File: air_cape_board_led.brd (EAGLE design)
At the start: 100 x 80 mm, 10 parts

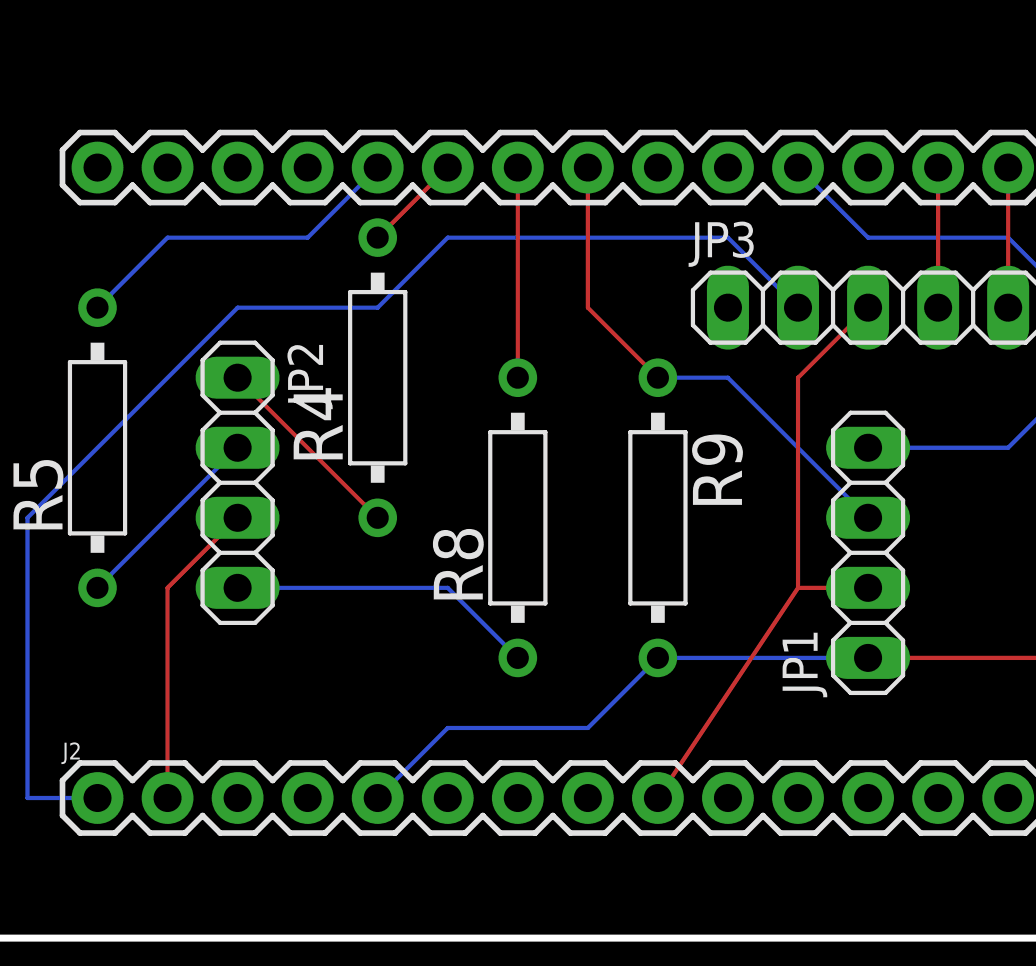
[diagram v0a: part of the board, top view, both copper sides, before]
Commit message: Fix issue with led power supply
- Should be VDD instead of GND
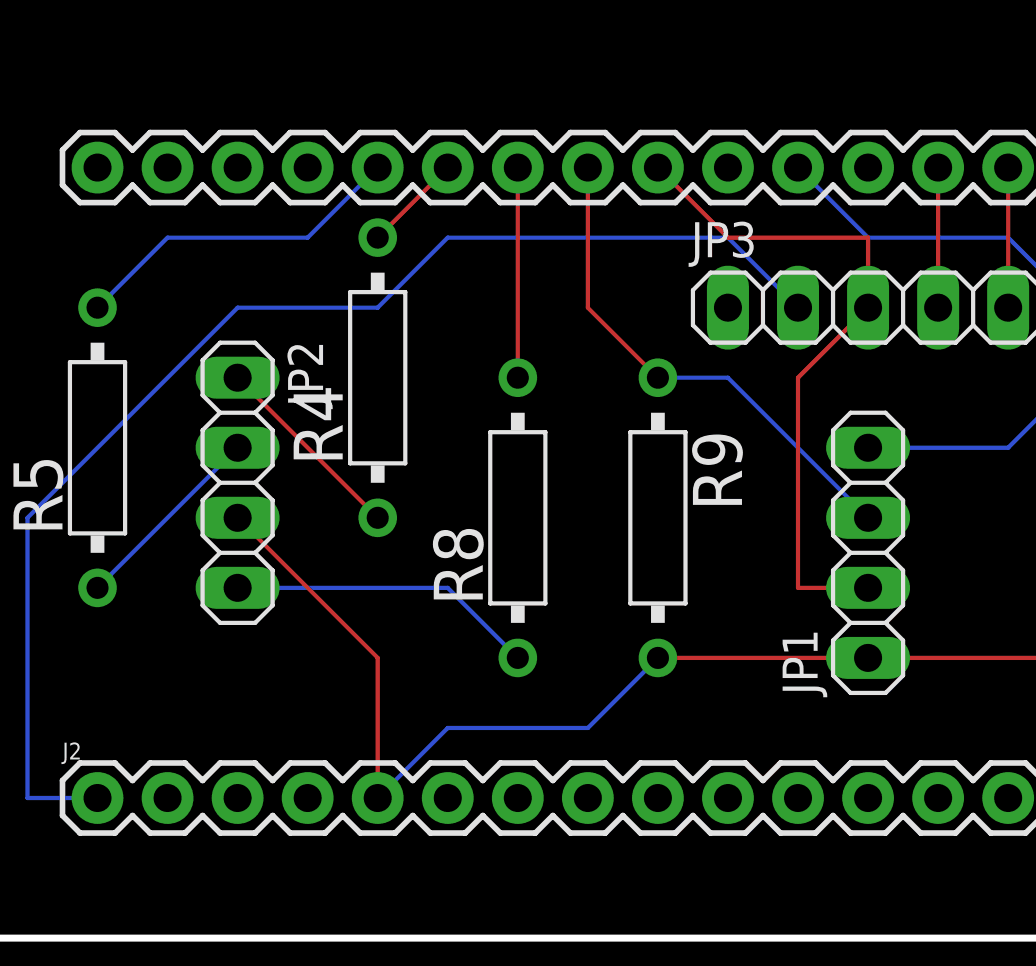
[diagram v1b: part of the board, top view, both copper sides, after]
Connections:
- new net SC: J2.9
- net +3V3: now also JP2.3
- net GND: no longer J2.9, JP2.3
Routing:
- net +3V3: track 27.5 -> 39.8 mm
- net GND: track 34.1 -> 25.0 mm
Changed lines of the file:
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@@
 <contactref element="J2" pad="2"/>
 <contactref element="J2" pad="6"/>
-<contactref element="J2" pad="9"/>
 <contactref element="JP1" pad="2"/>
-<contactref element="JP2" pad="3"/>
 <contactref element="JP3" pad="3"/>
-<wire x1="10.16" y1="12.7" x2="12.7" y2="15.24" width="0.1524" layer="1"/>
-<wire x1="10.16" y1="5.08" x2="10.16" y2="12.7" width="0.1524" layer="1"/>
-<wire x1="27.94" y1="5.08" x2="33.02" y2="12.7" width="0.1524" layer="1"/>
 <wire x1="33.02" y1="12.7" x2="35.56" y2="12.7" width="0.1524" layer="1"/>
 <wire x1="33.02" y1="20.32" x2="35.56" y2="22.86" width="0.1524" layer="1"/>
 <wire x1="33.02" y1="12.7" x2="33.02" y2="20.32" width="0.1524" layer="1"/>
-<wire x1="35.56" y1="22.86" x2="27.94" y2="27.94" width="0" layer="19" extent="1-1"/>
-<wire x1="20.32" y1="5.08" x2="27.94" y2="5.08" width="0" layer="19" extent="1-1"/>
+<wire x1="30.48" y1="25.4" x2="27.94" y2="27.94" width="0.1524" layer="1"/>
+<wire x1="35.56" y1="25.4" x2="30.48" y2="25.4" width="0.1524" layer="1"/>
+<wire x1="35.56" y1="22.86" x2="35.56" y2="25.4" width="0.1524" layer="1"/>
+<wire x1="20.32" y1="5.08" x2="33.02" y2="12.7" width="0" layer="19" extent="1-1"/>
 <wire x1="10.16" y1="5.08" x2="20.32" y2="5.08" width="0" layer="19" extent="1-1"/>
-<wire x1="10.16" y1="27.94" x2="12.7" y2="15.24" width="0" layer="19" extent="1-1"/>
+<wire x1="10.16" y1="27.94" x2="27.94" y2="27.94" width="0" layer="19" extent="1-1"/>
 </signal>
 <signal name="TX">
@@
 <contactref element="R9" pad="2"/>
 <contactref element="R10" pad="2"/>
-<wire x1="35.56" y1="10.16" x2="27.94" y2="10.16" width="0.1524" layer="16"/>
+<contactref element="JP2" pad="3"/>
+<wire x1="35.56" y1="10.16" x2="27.94" y2="10.16" width="0.1524" layer="1"/>
 <wire x1="35.56" y1="10.16" x2="43.18" y2="10.16" width="0.1524" layer="1"/>
-<wire x1="20.32" y1="7.62" x2="17.78" y2="5.08" width="0.1524" layer="16"/>
-<wire x1="25.4" y1="7.62" x2="20.32" y2="7.62" width="0.1524" layer="16"/>
-<wire x1="27.94" y1="10.16" x2="25.4" y2="7.62" width="0.1524" layer="16"/>
+<wire x1="17.78" y1="10.16" x2="12.7" y2="15.24" width="0.1524" layer="1"/>
+<wire x1="17.78" y1="5.08" x2="17.78" y2="10.16" width="0.1524" layer="1"/>
+<wire x1="25.4" y1="7.62" x2="27.94" y2="10.16" width="0.1524" layer="16"/>
+<wire x1="20.32" y1="7.62" x2="25.4" y2="7.62" width="0.1524" layer="16"/>
+<wire x1="17.78" y1="5.08" x2="20.32" y2="7.62" width="0.1524" layer="16"/>
 </signal>
 <signal name="+5V">
@@
 <wire x1="12.7" y1="20.32" x2="17.78" y2="15.24" width="0.1524" layer="1"/>
 </signal>
+<signal name="SC">
+<contactref element="J2" pad="9"/>
+</signal>
 </signals>
